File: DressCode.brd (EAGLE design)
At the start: 38.4 x 35.9 mm, 39 parts, among them M1 MIC9.7MM, M2 MIC6MM, Q1 2N7002, Q2 2N7002, Q3 2N7002, U1 MCP6S21, U2 MCP6S21, U3 MCP6G02, U4 PIC24FV32KA304-I/PT

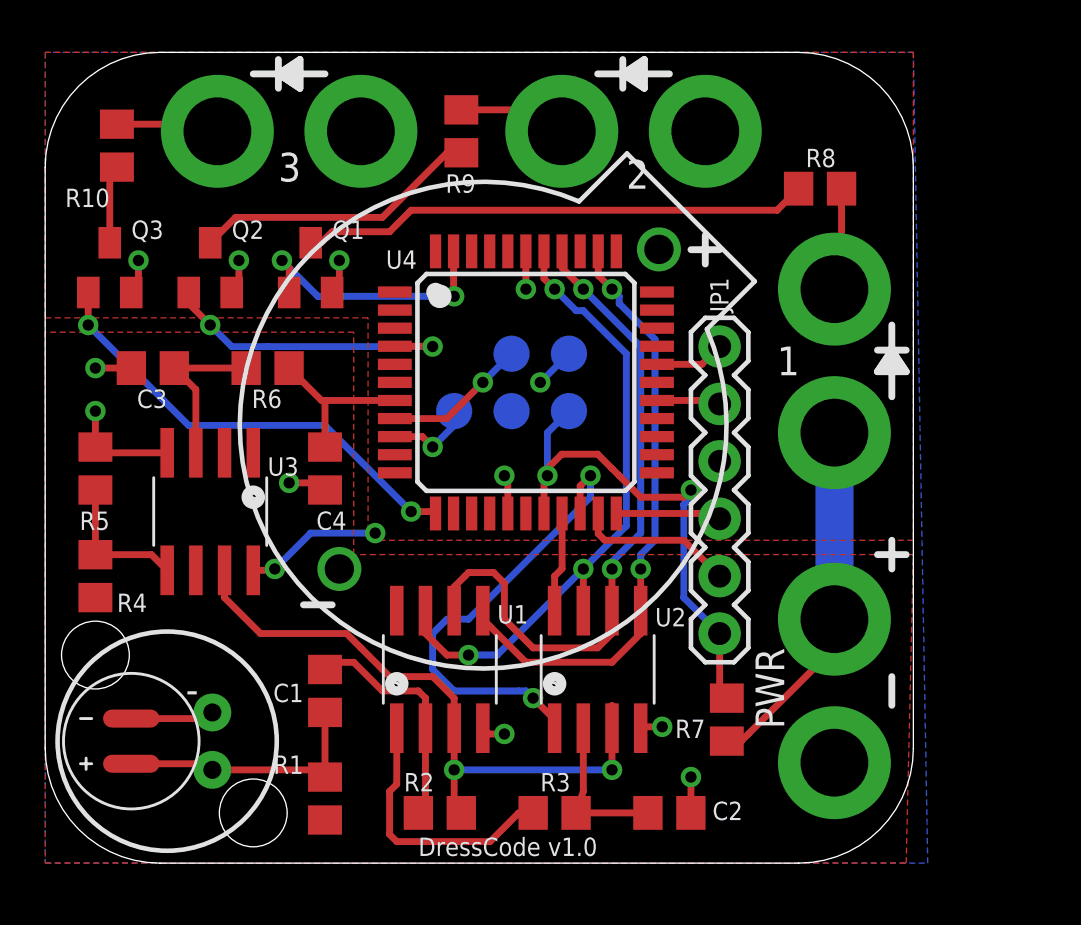
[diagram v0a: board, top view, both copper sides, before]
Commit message: JST connector added for LiPo power
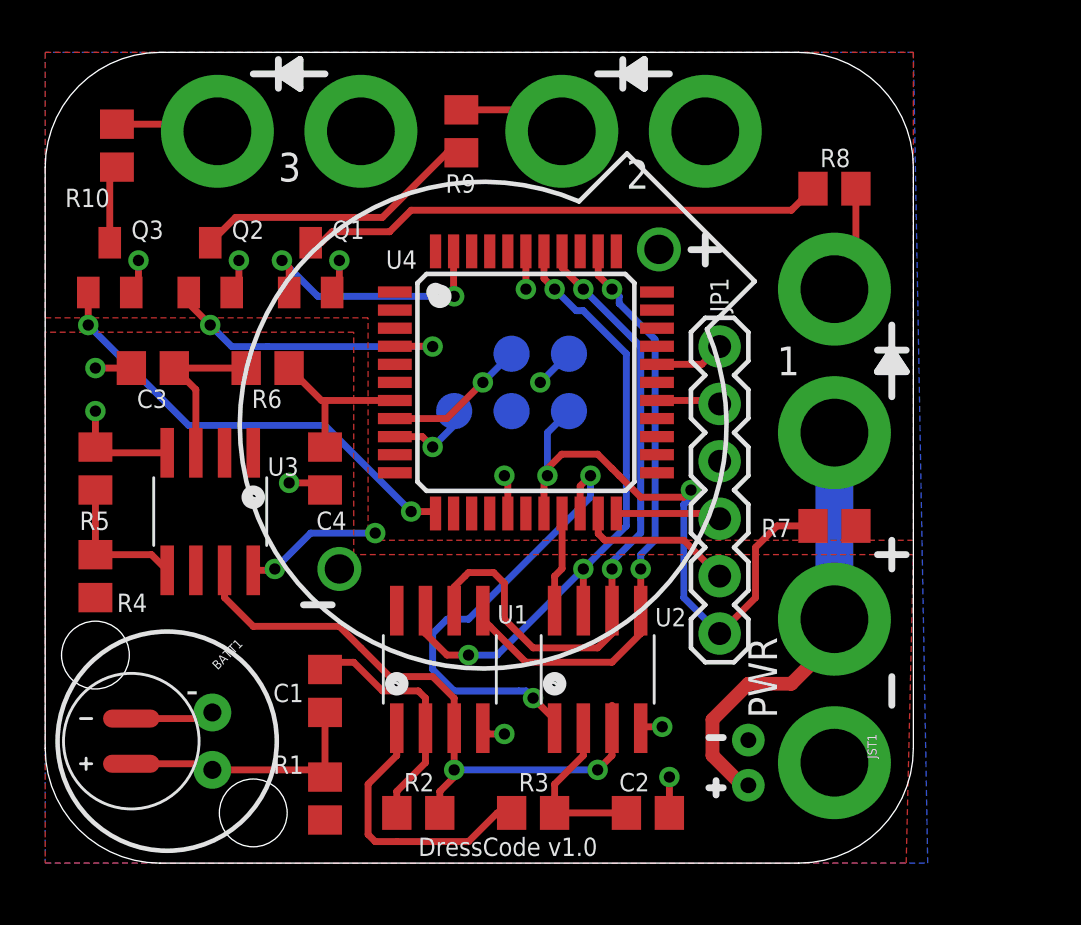
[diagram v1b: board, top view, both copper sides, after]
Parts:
- added JST1: (no value), SparkFun_08_2011:JST-2-PTH-NS
- moved R7 9.81 mm to (34.9, 14.9), turned to 0 degrees
- moved R3 0.95 mm to (21.6, 2.22)
- moved C2 0.95 mm to (26.7, 2.22)
- moved R2 0.95 mm to (16.5, 2.22)
- moved R8 0.63 mm to (34.9, 29.8)
- renumbered BAT1 to BATT1
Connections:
- net GND: now also JST1.1
- net VDD: now also JST1.2
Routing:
- net MCLR: track 23.0 -> 27.4 mm
- net VDD: track 23.9 -> 27.6 mm
- net N$2: track 10.4 -> 11.3 mm
- net N$9: track 22.6 -> 23.2 mm

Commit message: design now includes USB charger
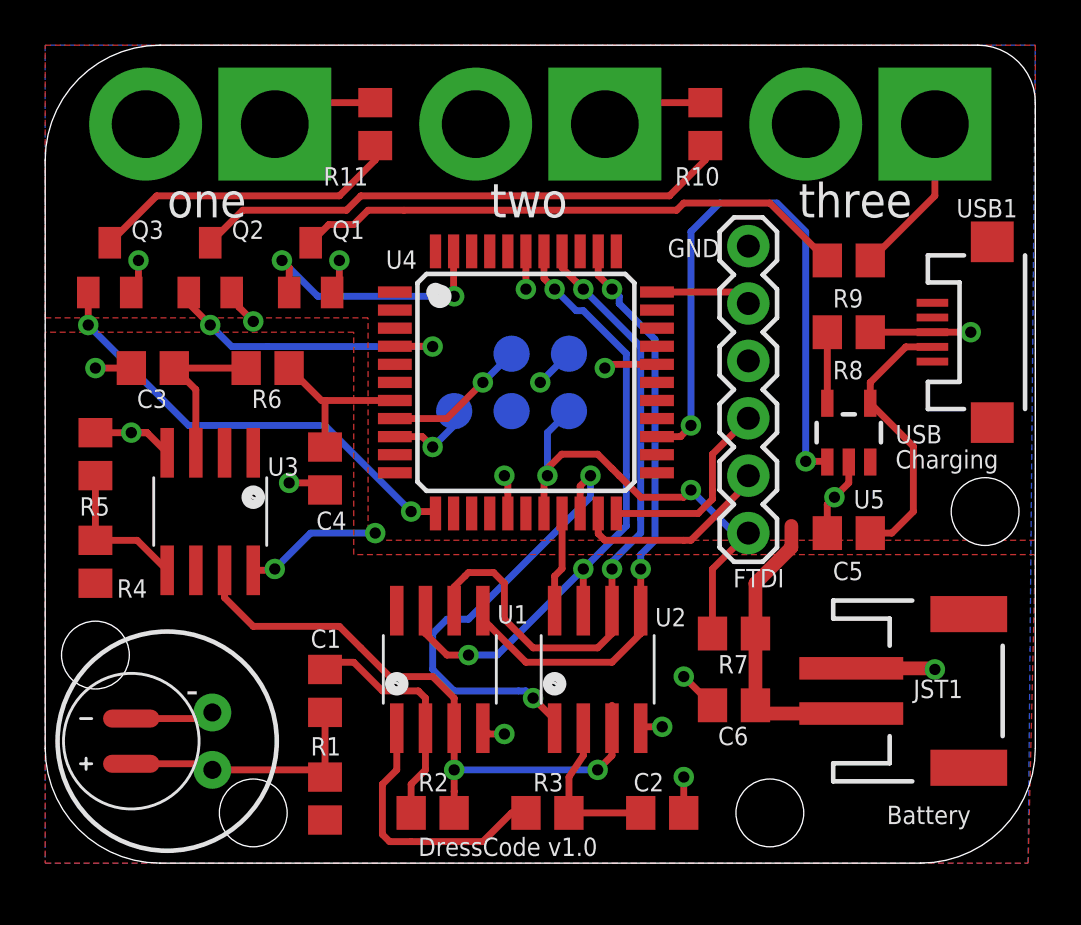
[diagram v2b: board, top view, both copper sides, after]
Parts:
- removed BATT1: (no value), SparkFun:BATTCOM_20MM_PTH
- removed U$1, U$2, U$3: DRESSCODE_SEW_PAD, x-io:DRESSCODE_SEW_PAD
- added C5, C6: 10u, rcl:C0805
- added R11: 100R, rcl:R0805
- added U$10: DRESSCODE_SEW_PADS, x-io:DRESSCODE_SEW_PAD_SQR
- added U5: MCP73832T-2ACI/OT, SparkFun_08_2011:SOT23-5
- added USB1: USB-MICROB, SparkFun_08_2011:USB-MICROB
- JST1: device SparkFun_08_2011:JST-2-PTH-NS -> SparkFun_08_2011:JST-2-SMD
- R8: value 100R -> 2.2k
- U$4, U$5, U$6: value DRESSCODE_SEW_PAD -> DRESSCODE_SEW_PADC; device x-io:DRESSCODE_SEW_PAD -> x-io:DRESSCODE_SEW_PAD_CIRC
- U$7, U$8: value DRESSCODE_SEW_PAD -> DRESSCODE_SEW_PADS; device x-io:DRESSCODE_SEW_PAD -> x-io:DRESSCODE_SEW_PAD_SQR
- moved U$7 28.6 mm to (39.4, 32.7), turned to 0 degrees
- moved R10 26.1 mm to (29.2, 32.7)
- moved U$8 24.1 mm to (24.8, 32.7), turned to 0 degrees
- moved R9 18.1 mm to (35.6, 26.7), turned to 0 degrees
- moved U$4 13.7 mm to (33.7, 32.7)
- moved U$9 11.0 mm to (3.67, 4.35)
- moved U$6 10.2 mm to (19.1, 32.7)
- moved U$5 9.53 mm to (4.45, 32.7)
- moved JST1 8.84 mm to (39.4, 7.62)
- moved R7 6.51 mm to (30.5, 10.2)
- moved R8 6.38 mm to (35.6, 23.5), turned to 180 degrees
- moved JP1 4.62 mm to (31.1, 27.3)
- moved R3 0.64 mm to (22.2, 2.22)
- moved R4 0.64 mm to (2.22, 13.3)
- moved R5 0.64 mm to (2.22, 18.1)
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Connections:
- removed net RC2: JP1.2, U4.27
- new net N$15: R8.2, U5.5
- new net RB4: JP1.2, U4.33
- new net STAT: U4.25, U5.1
- new net USB1: C5.2, U5.4, USB1.D-
- net GND: now also C5.1, C6.1, R8.1, U5.2, USB1.D+; no longer BATT1.2, U$7.1
- net N$10: now also R10.1; no longer R9.1
- net N$11: now also R11.1; no longer R10.1
- net N$12: now also R9.2, U$7.1; no longer R8.2, U$1.1
- net N$13: now also R10.2, U$8.1; no longer R9.2, U$2.1
- net N$14: now also R11.2, U$10.1; no longer R10.2, U$3.1
- net N$9: now also R9.1; no longer R8.1
- net VDD: now also C6.2, U5.3; no longer BATT1.1, U$8.1
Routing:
- net STAT: track 0.00 -> 27.6 mm, vias 0 -> 2
- net GND: track 26.7 -> 40.1 mm, vias 11 -> 16
- net USB1: track 0.00 -> 12.2 mm
- net N$10: track 12.8 -> 24.1 mm
- net N$11: track 3.48 -> 13.9 mm
- net MCLR: track 27.4 -> 21.3 mm
- net VDD: track 27.6 -> 22.2 mm
- net RB4: track 0.00 -> 4.25 mm
- net FTDI_TX: track 4.67 -> 8.75 mm
- net N$15: track 0.00 -> 3.14 mm
- net RC2: track 2.84 -> 0.00 mm
- net N$12: track 4.84 -> 7.22 mm
- net FTDI_RX: track 7.04 -> 9.03 mm
- net N$9: track 23.2 -> 24.6 mm
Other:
- board size 38.4 x 35.9 mm -> 43.8 x 36.2 mm
- board text added: "Battery"
- board text added: "Charging"
- board text added: "FTDI"
- board text added: "GND"
- board text added: "USB"
- board text added: "one"
- board text added: "three"
- board text added: "two"
- board text removed: "1"
- board text removed: "2"
- board text removed: "3"
- board text removed: "PWR"

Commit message: added power switch
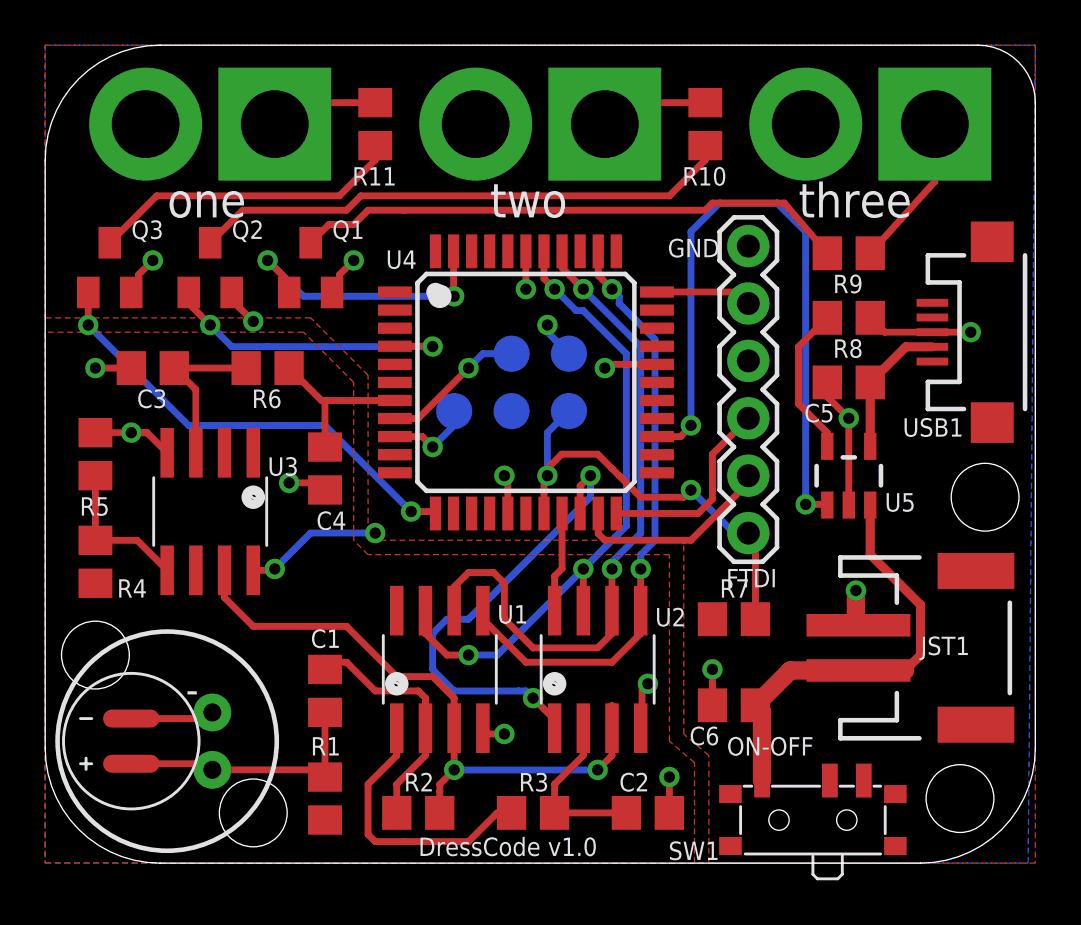
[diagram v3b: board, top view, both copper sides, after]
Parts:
- added SW1: PCM12SMTR, SparkFun0modified:PCM12SMTR
- moved C5 6.67 mm to (35.6, 21.3)
- moved JST1 1.93 mm to (39.7, 9.53)
- moved U5 1.91 mm to (35.6, 17.1)
- moved R3 0.64 mm to (21.6, 2.22)
- moved R7 0.63 mm to (30.5, 10.8), turned to 180 degrees
- moved C2 0.63 mm to (26.7, 2.22)
- moved R2 0.63 mm to (16.5, 2.22)
- moved R8 0.63 mm to (35.6, 24.1)
- moved R9 0.32 mm to (35.6, 27.0)
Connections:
- new net BATT: C6.2, JST1.2, SW1.1, U5.3
- net VDD: now also SW1.2; no longer C6.2, JST1.2, U5.3
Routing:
- net BATT: track 0.00 -> 19.2 mm
- net VDD: track 22.2 -> 7.74 mm
- net USB1: track 12.2 -> 6.23 mm
- net N$15: track 3.14 -> 6.74 mm
- net STAT: track 27.6 -> 29.5 mm
- net GND: track 40.1 -> 41.8 mm
- net MCLR: track 21.3 -> 20.1 mm
- net PWM1: track 11.8 -> 12.7 mm
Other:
- board text added: "OFF"
- board text added: "ON"
- board text added: "ON-OFF"
- board text removed: "Battery"
- board text removed: "Charging"
- board text removed: "USB"

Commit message: added OSH logo
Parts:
- added U$1: (no value), x-io:OSHW_LOGO_6MM_BOTTOM
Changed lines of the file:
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@@
 <hole x="9.2075" y="2.2225" drill="3"/>
 <text x="16.51" y="0.3175" size="0.8128" layer="121" font="vector">DressCode v1.0</text>
-<text x="42" y="6" size="0.8128" layer="122" font="vector" rot="MR0">Seb Madgwick</text>
-<text x="42" y="8" size="0.8128" layer="122" font="vector" rot="MR0">DressCode v1.0</text>
+<text x="41.91" y="5.3975" size="0.8128" layer="122" font="vector" rot="MR0">Seb Madgwick</text>
+<text x="41.91" y="6.985" size="0.8128" layer="122" font="vector" rot="MR0">DressCode v1.0</text>
 <circle x="17.4625" y="25.0825" radius="0.3175" width="0.4064" layer="121"/>
 <circle x="15.5575" y="7.9375" radius="0.3175" width="0.4064" layer="121"/>
@@
 <attribute name="VALUE" x="39.0525" y="0.635" size="0.8128" layer="27"/>
 </element>
+<element name="U$1" library="x-io" package="OSHW_LOGO_6MM_BOTTOM" value="" x="41.91" y="8.89" rot="MR0"/>
 </elements>
 <signals>
